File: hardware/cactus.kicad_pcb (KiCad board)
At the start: 2 copper layers, 76.5 x 38.1 mm, 24 parts, among them SW1 SW_Push, U1 WeMos_Battery_Shield, U2 WeMos_D1_mini, U3 74HC595, U4 Si7021_breakout

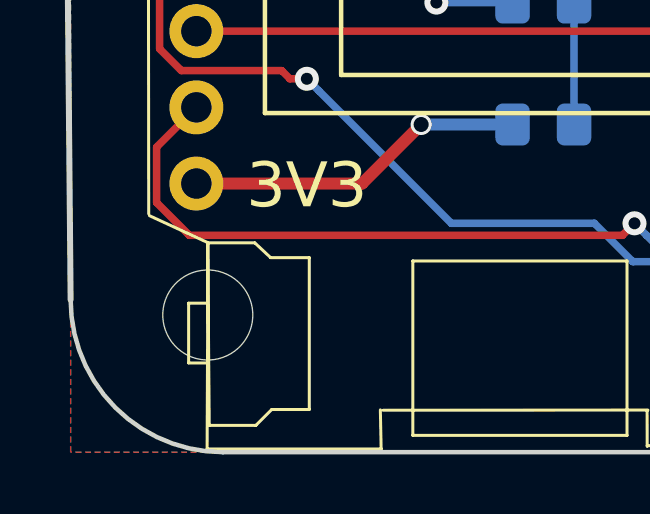
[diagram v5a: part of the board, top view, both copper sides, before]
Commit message: [mech] Add dimensions to the drawings layer
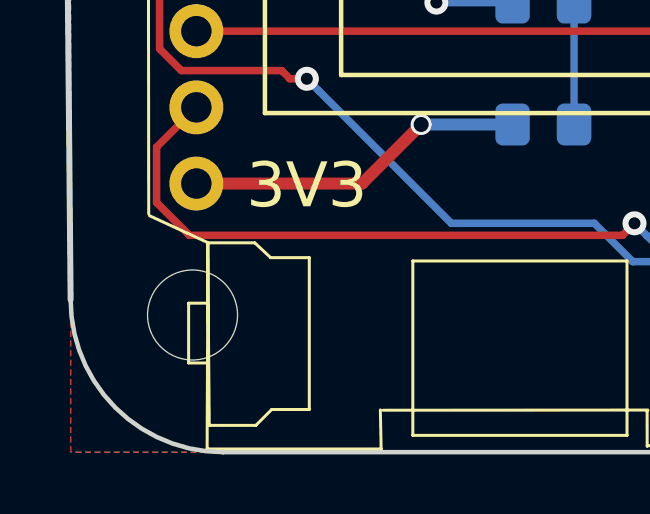
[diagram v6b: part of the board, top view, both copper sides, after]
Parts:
- moved REF** 0.51 mm to (118.4, 84.3)
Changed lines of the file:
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@@
   (general
     (thickness 1.6)
-    (drawings 32)
+    (drawings 35)
     (tracks 179)
     (zones 0)
@@
   (page A4)
   (layers
-    (0 F.Cu signal hide)
-    (31 B.Cu signal hide)
+    (0 F.Cu signal)
+    (31 B.Cu signal)
     (32 B.Adhes user)
     (33 F.Adhes user)
     (34 B.Paste user)
-    (35 F.Paste user)
+    (35 F.Paste user hide)
     (36 B.SilkS user)
-    (37 F.SilkS user)
+    (37 F.SilkS user hide)
     (38 B.Mask user)
-    (39 F.Mask user)
+    (39 F.Mask user hide)
     (40 Dwgs.User user)
     (41 Cmts.User user)
@@
     (45 Margin user)
     (46 B.CrtYd user)
-    (47 F.CrtYd user)
-    (48 B.Fab user)
-    (49 F.Fab user)
+    (47 F.CrtYd user hide)
+    (48 B.Fab user hide)
+    (49 F.Fab user hide)
   )
   (setup
@@
     (tags "Logo Symbol OSHW")
     (attr virtual)
-    (fp_text reference LOGO (at -5.969 0.254 180) (layer B.SilkS) hide
-      (effects (font (size 1 1) (thickness 0.15)) (justify mirror))
-    )
-    (fp_text value OSHW-Logo2_7.3x6mm_SilkScreen (at 0 3.81 180) (layer B.Fab) hide
-      (effects (font (size 1 1) (thickness 0.15)) (justify mirror))
+    (fp_text reference LOGO (at 6.096 0.127 180) (layer B.SilkS) hide
+      (effects (font (size 1 1) (thickness 0.15)) (justify mirror))
+    )
+    (fp_text value OSHW-Logo2_7.3x6mm_SilkScreen (at 0.127 2.286) (layer B.Fab) hide
+      (effects (font (size 0.5 0.5) (thickness 0.125)) (justify mirror))
     )
     (fp_poly (pts (xy 0.10391 2.757652) (xy 0.182454 2.757222) (xy 0.239298 2.756058) (xy 0.278105 2.753793)
@@
   )
   (module MountingHole:MountingHole_3mm (layer F.Cu)
-    (at 118.872 84.328)
+    (at 118.364 84.328)
     (descr "Mounting Hole 3mm, no annular")
     (tags "mounting hole 3mm no annular")
@@
     (pad 1 np_thru_hole circle (at 0 0) (size 3 3) (drill 3) (layers *.Cu *.Mask))
   )
+  (dimension 3.2004 (width 0.3) (layer Dwgs.User)
+    (gr_text "3.200 mm" (at 118.3386 93.921) (layer Dwgs.User)
+      (effects (font (size 1.5 1.5) (thickness 0.3)))
+    )
+    (feature1 (pts (xy 116.7384 84.4296) (xy 116.7384 92.407421)))
+    (feature2 (pts (xy 119.9388 84.4296) (xy 119.9388 92.407421)))
+    (crossbar (pts (xy 119.9388 91.821) (xy 116.7384 91.821)))
+    (arrow1a (pts (xy 116.7384 91.821) (xy 117.864904 91.234579)))
+    (arrow1b (pts (xy 116.7384 91.821) (xy 117.864904 92.407421)))
+    (arrow2a (pts (xy 119.9388 91.821) (xy 118.812296 91.234579)))
+    (arrow2b (pts (xy 119.9388 91.821) (xy 118.812296 92.407421)))
+  )
+  (dimension 38.2524 (width 0.3) (layer Dwgs.User)
+    (gr_text "38.252 mm" (at 195.2162 69.9008 90) (layer Dwgs.User)
+      (effects (font (size 1.5 1.5) (thickness 0.3)))
+    )
+    (feature1 (pts (xy 184.404 50.7746) (xy 193.702621 50.7746)))
+    (feature2 (pts (xy 184.404 89.027) (xy 193.702621 89.027)))
+    (crossbar (pts (xy 193.1162 89.027) (xy 193.1162 50.7746)))
+    (arrow1a (pts (xy 193.1162 50.7746) (xy 193.702621 51.901104)))
+    (arrow1b (pts (xy 193.1162 50.7746) (xy 192.529779 51.901104)))
+    (arrow2a (pts (xy 193.1162 89.027) (xy 193.702621 87.900496)))
+    (arrow2b (pts (xy 193.1162 89.027) (xy 192.529779 87.900496)))
+  )
+  (dimension 76.174617 (width 0.3) (layer Dwgs.User)
+    (gr_text "76.175 mm" (at 152.152016 46.897333 0.03820991732) (layer Dwgs.User)
+      (effects (font (size 1.5 1.5) (thickness 0.3)))
+    )
+    (feature1 (pts (xy 114.0714 56.9468) (xy 114.065724 48.436312)))
+    (feature2 (pts (xy 190.246 56.896) (xy 190.240324 48.385512)))
+    (crossbar (pts (xy 190.240716 48.971933) (xy 114.066116 49.022733)))
+    (arrow1a (pts (xy 114.066116 49.022733) (xy 115.192228 48.435561)))
+    (arrow1b (pts (xy 114.066116 49.022733) (xy 115.193011 49.608402)))
+    (arrow2a (pts (xy 190.240716 48.971933) (xy 189.113821 48.386264)))
+    (arrow2b (pts (xy 190.240716 48.971933) (xy 189.114604 49.559105)))
+  )
   (gr_text QE (at 157.607 62.865) (layer B.SilkS)
